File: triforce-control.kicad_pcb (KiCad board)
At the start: 2 copper layers, 75 x 86 mm, 14 parts, among them CON1 Conn_01x08, CON2 Conn_01x08, CON3 CON_ESC_W1, CON4 CON_ESC_W2, CON5 CON_ESC_W3, CON6 CON_ESC_D1, CON7 CON_ESC_D2, CON8 CON_ESC_D3, CON9 Conn_01x04, U1 ADAFRUIT_HUZZAH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

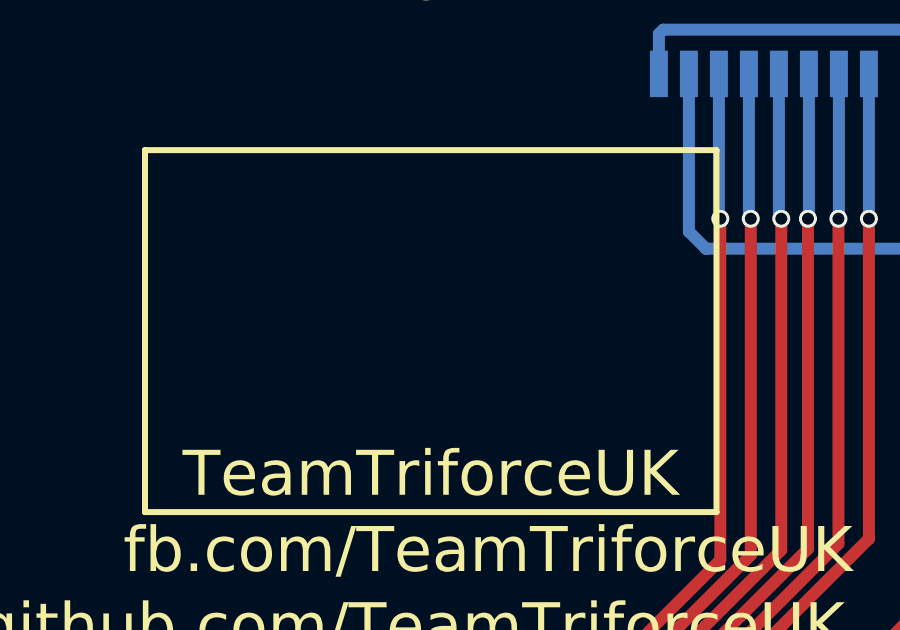
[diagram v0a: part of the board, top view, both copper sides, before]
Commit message: Added Triforce logo and JST SH models.
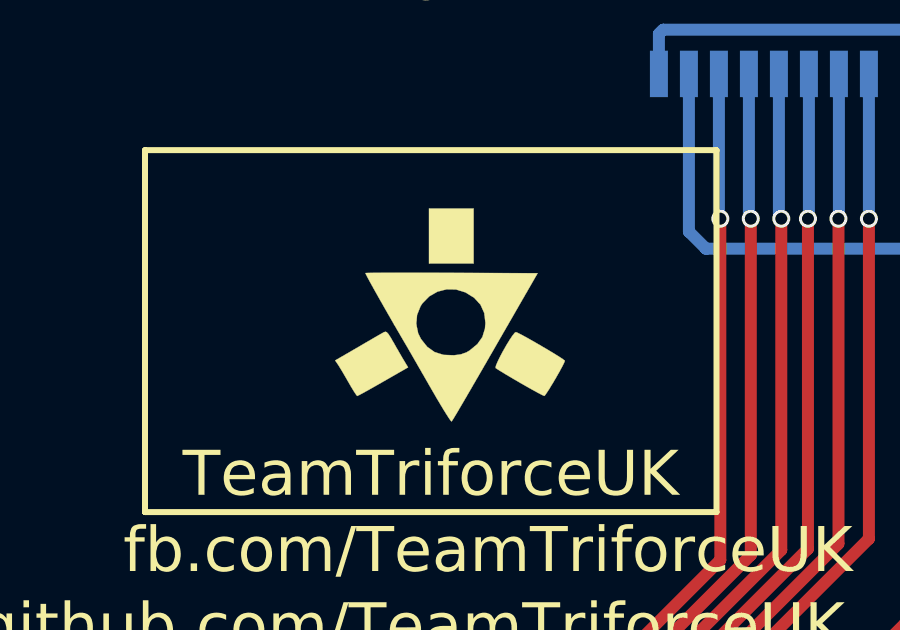
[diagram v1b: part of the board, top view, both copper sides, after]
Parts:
- added G***: LOGO, mbed:logo_small, F.Cu at (134.6, 55.2)
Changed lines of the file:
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@@
 (kicad_pcb (version 4) (host pcbnew 4.0.7-e2-6376~58~ubuntu16.04.1)
   (general
-    (links 91)
+    (links 0)
     (no_connects 1)
     (area 114.359999 40.909999 189.510001 127.060001)
@@
     (tracks 305)
     (zones 0)
-    (modules 14)
+    (modules 15)
     (nets 72)
   )
@@
     )
   )
+  (module mbed:logo_small (layer F.Cu)
+    (at 134.62 55.245)
+    (fp_text reference G*** (at 0 0) (layer F.SilkS) hide
+      (effects (font (thickness 0.3)))
+    )
+    (fp_text value LOGO (at 0.75 0) (layer F.SilkS) hide
+      (effects (font (thickness 0.3)))
+    )
+    (fp_poly (pts (xy -0.861467 -1.628171) (xy -0.36223 -1.626806) (xy 0.066973 -1.625113) (xy 2.927795 -1.612304)
+      (xy 1.942747 0.099219) (xy 1.566002 0.753454) (xy 1.236435 1.324966) (xy 0.952037 1.817199)
+      (xy 0.710799 2.233601) (xy 0.510714 2.577614) (xy 0.349771 2.852686) (xy 0.225964 3.062261)
+      (xy 0.137282 3.209784) (xy 0.081717 3.298702) (xy 0.058198 3.331631) (xy 0.025863 3.299073)
+      (xy -0.048536 3.190789) (xy -0.158361 3.017498) (xy -0.296978 2.789919) (xy -0.45775 2.518772)
+      (xy -0.634042 2.214776) (xy -0.644922 2.195806) (xy -0.827709 1.877073) (xy -0.999435 1.577942)
+      (xy -1.15237 1.311848) (xy -1.278788 1.092227) (xy -1.370963 0.932516) (xy -1.419752 0.84855)
+      (xy -1.626972 0.4944) (xy -1.834648 0.13656) (xy -1.863463 0.086534) (xy -1.117272 0.086534)
+      (xy -1.054914 0.388357) (xy -0.964282 0.574638) (xy -0.754478 0.839692) (xy -0.505655 1.016545)
+      (xy -0.209415 1.109376) (xy 0.137939 1.122668) (xy 0.370122 1.092183) (xy 0.553448 1.026106)
+      (xy 0.658566 0.964242) (xy 0.916798 0.753122) (xy 1.084861 0.515258) (xy 1.171034 0.236236)
+      (xy 1.186851 0.04461) (xy 1.148874 -0.281791) (xy 1.023581 -0.561177) (xy 0.811279 -0.793079)
+      (xy 0.520898 -0.972973) (xy 0.209093 -1.069173) (xy -0.108663 -1.074897) (xy -0.41394 -0.995844)
+      (xy -0.688309 -0.837714) (xy -0.913341 -0.606207) (xy -0.976493 -0.509828) (xy -1.091222 -0.220917)
+      (xy -1.117272 0.086534) (xy -1.863463 0.086534) (xy -2.036911 -0.214584) (xy -2.22789 -0.548651)
+      (xy -2.401716 -0.855256) (xy -2.552519 -1.124017) (xy -2.674429 -1.34455) (xy -2.761575 -1.506471)
+      (xy -2.808088 -1.599399) (xy -2.814023 -1.617747) (xy -2.76211 -1.621219) (xy -2.619809 -1.624067)
+      (xy -2.395948 -1.62627) (xy -2.099354 -1.627804) (xy -1.738858 -1.628647) (xy -1.323286 -1.628777)
+      (xy -0.861467 -1.628171)) (layer F.SilkS) (width 0.01))
+    (fp_poly (pts (xy -2.102537 0.352928) (xy -2.04582 0.414758) (xy -1.967134 0.53794) (xy -1.868599 0.709245)
+      (xy -1.750056 0.917277) (xy -1.633713 1.118789) (xy -1.539213 1.279841) (xy -1.514454 1.321161)
+      (xy -1.390463 1.526111) (xy -2.222156 2.00329) (xy -2.481427 2.151137) (xy -2.711046 2.280349)
+      (xy -2.897272 2.383334) (xy -3.026364 2.452502) (xy -3.084581 2.480261) (xy -3.085892 2.480469)
+      (xy -3.121943 2.440006) (xy -3.194501 2.33055) (xy -3.292171 2.169997) (xy -3.378019 2.021582)
+      (xy -3.496304 1.81562) (xy -3.60641 1.628723) (xy -3.693219 1.486319) (xy -3.730298 1.429209)
+      (xy -3.822493 1.295722) (xy -3.461539 1.086921) (xy -3.238749 0.957704) (xy -2.980778 0.807578)
+      (xy -2.738008 0.665871) (xy -2.703711 0.645803) (xy -2.515602 0.536251) (xy -2.349814 0.440703)
+      (xy -2.232294 0.374072) (xy -2.202794 0.357882) (xy -2.150467 0.338589) (xy -2.102537 0.352928)) (layer F.SilkS) (width 0.01))
+    (fp_poly (pts (xy 2.263897 0.37481) (xy 2.393107 0.440608) (xy 2.571508 0.53783) (xy 2.78282 0.656955)
+      (xy 3.010764 0.788463) (xy 3.239059 0.922833) (xy 3.451425 1.050544) (xy 3.631582 1.162075)
+      (xy 3.76325 1.247906) (xy 3.830149 1.298516) (xy 3.835249 1.306176) (xy 3.810723 1.372942)
+      (xy 3.746767 1.500687) (xy 3.654718 1.670011) (xy 3.545916 1.861511) (xy 3.431697 2.055788)
+      (xy 3.323401 2.233439) (xy 3.232365 2.375063) (xy 3.169929 2.46126) (xy 3.150195 2.478378)
+      (xy 3.093056 2.45465) (xy 2.965134 2.388714) (xy 2.781208 2.288598) (xy 2.556059 2.162326)
+      (xy 2.33909 2.037981) (xy 2.089308 1.892314) (xy 1.868077 1.761103) (xy 1.69035 1.653391)
+      (xy 1.571081 1.578225) (xy 1.526835 1.546679) (xy 1.531662 1.487937) (xy 1.579598 1.36539)
+      (xy 1.659723 1.198448) (xy 1.761115 1.006521) (xy 1.872852 0.809022) (xy 1.984014 0.625361)
+      (xy 2.083679 0.474948) (xy 2.160926 0.377196) (xy 2.200159 0.349958) (xy 2.263897 0.37481)) (layer F.SilkS) (width 0.01))
+    (fp_poly (pts (xy 0.79375 -1.934765) (xy -0.694531 -1.934765) (xy -0.694531 -3.770312) (xy 0.79375 -3.770312)
+      (xy 0.79375 -1.934765)) (layer F.SilkS) (width 0.01))
+  )
   (gr_line (start 119.38 67.945) (end 119.38 70.485) (layer F.SilkS) (width 0.2))
